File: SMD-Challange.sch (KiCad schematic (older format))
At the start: 19 parts, among them SW1 SW_DPDT_x2, U1 NE555, U2 4017

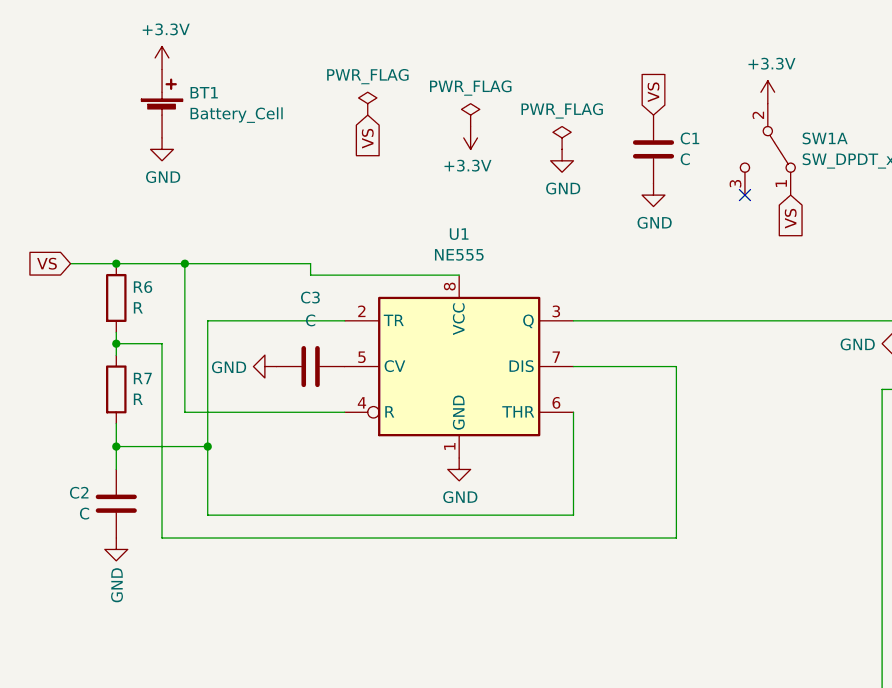
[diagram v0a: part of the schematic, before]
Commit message: update component values for ne555 oscillator
Frequency is now 4.8 Hz

Signed-off-by: Thomas Schmid <tom@binary-kitchen.de>
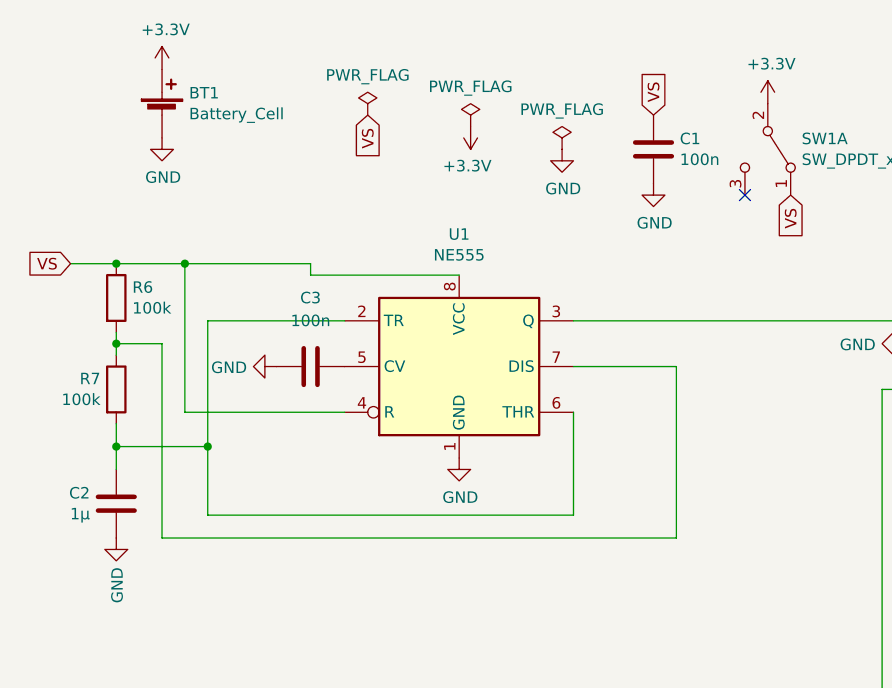
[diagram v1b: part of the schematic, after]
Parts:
- C1, C3: value C -> 100n
- C2: value C -> 1µ
- R6, R7: value R -> 100k
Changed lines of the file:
@@
 P 4600 1500
 F 0 "C1" H 4485 1454 50  0000 R CNN
-F 1 "C" H 4485 1545 50  0000 R CNN
+F 1 "100n" H 4485 1545 50  0000 R CNN
 F 2 "Capacitor_SMD:C_0805_2012Metric_Pad1.15x1.40mm_HandSolder" H 4638 1350 50  0001 C CNN
 F 3 "~" H 4600 1500 50  0001 C CNN
@@
 P 3100 2450
 F 0 "C3" V 2800 2450 50  0000 C CNN
-F 1 "C" V 2900 2450 50  0000 C CNN
+F 1 "100n" V 2900 2450 50  0000 C CNN
 F 2 "Capacitor_SMD:C_0805_2012Metric_Pad1.15x1.40mm_HandSolder" H 3138 2300 50  0001 C CNN
 F 3 "~" H 3100 2450 50  0001 C CNN
@@
 P 2250 2150
 F 0 "R6" H 2320 2196 50  0000 L CNN
-F 1 "R" H 2320 2105 50  0000 L CNN
+F 1 "100k" H 2320 2105 50  0000 L CNN
 F 2 "Resistor_SMD:R_0805_2012Metric_Pad1.15x1.40mm_HandSolder" V 2180 2150 50  0001 C CNN
 F 3 "~" H 2250 2150 50  0001 C CNN
@@
 U 1 1 5BE5B5C6
 P 2250 2550
-F 0 "R7" H 2320 2596 50  0000 L CNN
-F 1 "R" H 2320 2505 50  0000 L CNN
+F 0 "R7" H 2181 2596 50  0000 R CNN
+F 1 "100k" H 2181 2505 50  0000 R CNN
 F 2 "Resistor_SMD:R_0805_2012Metric_Pad1.15x1.40mm_HandSolder" V 2180 2550 50  0001 C CNN
 F 3 "~" H 2250 2550 50  0001 C CNN
@@
 P 2250 3050
 F 0 "C2" H 2365 3004 50  0000 L CNN
-F 1 "C" H 2365 3095 50  0000 L CNN
+F 1 "1µ" H 2365 3095 50  0000 L CNN
 F 2 "Capacitor_SMD:C_0805_2012Metric_Pad1.15x1.40mm_HandSolder" H 2288 2900 50  0001 C CNN
 F 3 "~" H 2250 3050 50  0001 C CNN

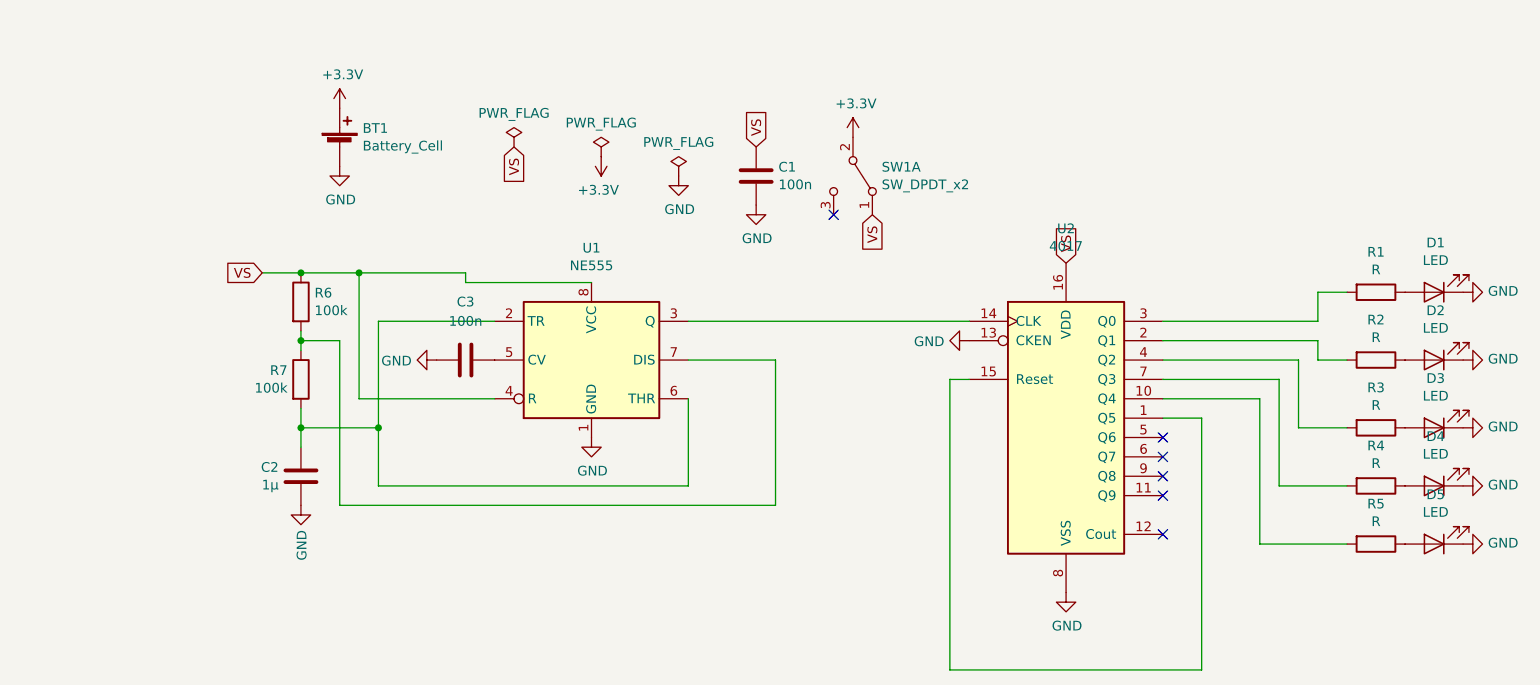
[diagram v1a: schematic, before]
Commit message: cleanup schematic and add title
Signed-off-by: Thomas Schmid <tom@binary-kitchen.de>
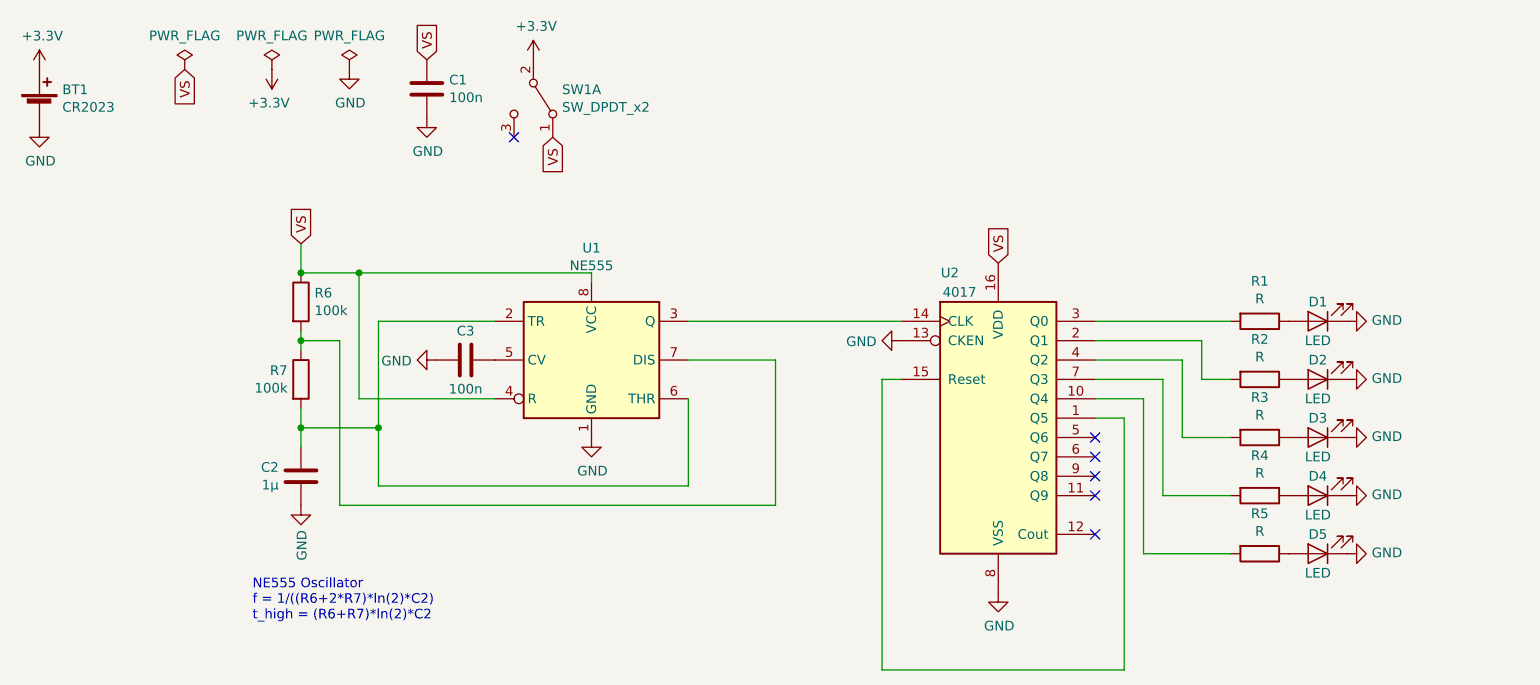
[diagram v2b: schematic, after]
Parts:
- BT1: value Battery_Cell -> CR2023
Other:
- note added: "NE555 Oscillator\nf = 1/((R6+2*R7)*ln(2)*C2)\nt_high = (R6+R7)*ln(2)*C2"
- moved on the sheet: BT1, C1, D1, D2, D3, D4, D5, R1, R2, R3, R4, R5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

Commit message: added custom footprints for smd 0201 and 01005 for hand-soldering
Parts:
- D4, D5: footprint LED_SMD:LED_0201_0603Metric -> SMD-Challange:LED_0201_0603Metric_hand_soldering
- R4: footprint LED_SMD:LED_0201_0603Metric -> SMD-Challange:R_0201_0603Metric_hand_soldering
- R5: footprint LED_SMD:LED_01005_0402Metric -> SMD-Challange:R_01005_0402Metric_hand_soldering
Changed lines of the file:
@@
 F 0 "D4" H 7500 3050 50  0000 C CNN
 F 1 "LED" H 7500 3250 50  0000 C CNN
-F 2 "LED_SMD:LED_0201_0603Metric" H 7500 3150 50  0001 C CNN
+F 2 "SMD-Challange:LED_0201_0603Metric_hand_soldering" H 7500 3150 50  0001 C CNN
 F 3 "~" H 7500 3150 50  0001 C CNN
 	1    7500 3150
@@
 F 0 "D5" H 7500 3350 50  0000 C CNN
 F 1 "LED" H 7500 3550 50  0000 C CNN
-F 2 "LED_SMD:LED_0201_0603Metric" H 7500 3450 50  0001 C CNN
+F 2 "SMD-Challange:LED_0201_0603Metric_hand_soldering" H 7500 3450 50  0001 C CNN
 F 3 "~" H 7500 3450 50  0001 C CNN
 	1    7500 3450
@@
 F 0 "R4" V 6993 3150 50  0000 C CNN
 F 1 "R" V 7084 3150 50  0000 C CNN
-F 2 "LED_SMD:LED_0201_0603Metric" V 7130 3150 50  0001 C CNN
+F 2 "SMD-Challange:R_0201_0603Metric_hand_soldering" V 7130 3150 50  0001 C CNN
 F 3 "~" H 7200 3150 50  0001 C CNN
 	1    7200 3150
@@
 F 0 "R5" V 6993 3450 50  0000 C CNN
 F 1 "R" V 7084 3450 50  0000 C CNN
-F 2 "LED_SMD:LED_01005_0402Metric" V 7130 3450 50  0001 C CNN
+F 2 "SMD-Challange:R_01005_0402Metric_hand_soldering" V 7130 3450 50  0001 C CNN
 F 3 "~" H 7200 3450 50  0001 C CNN
 	1    7200 3450

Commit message: changed some footprints and made the surface printing nicer
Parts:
- D1: footprint LED_SMD:LED_0805_2012Metric_Pad1.15x1.40mm_HandSolder -> SMD-Challange:LED_0805_2012Metric_Pad1.15x1.40mm_HandSolder_simple_drawing
- D2: footprint LED_SMD:LED_0603_1608Metric_Pad1.05x0.95mm_HandSolder -> SMD-Challange:LED_0603_1608Metric_Pad1.05x0.95mm_HandSolder_simple_drawing
- R1: footprint LED_SMD:LED_0805_2012Metric_Pad1.15x1.40mm_HandSolder -> Resistor_SMD:R_0805_2012Metric_Pad1.15x1.40mm_HandSolder
- R2: footprint LED_SMD:LED_0603_1608Metric_Pad1.05x0.95mm_HandSolder -> Resistor_SMD:R_0603_1608Metric_Pad1.05x0.95mm_HandSolder
- R3: footprint LED_SMD:LED_0402_1005Metric -> Resistor_SMD:R_0402_1005Metric
- U2: footprint Package_SO:SOP-16_4.4x10.4mm_P1.27mm -> SMD-Challange:SOP-16_4.4x10.4mm_P1.27mm_simple_drawing
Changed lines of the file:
@@
 F 0 "D1" H 7500 2150 50  0000 C CNN
 F 1 "LED" H 7500 2350 50  0000 C CNN
-F 2 "LED_SMD:LED_0805_2012Metric_Pad1.15x1.40mm_HandSolder" H 7500 2250 50  0001 C CNN
+F 2 "SMD-Challange:LED_0805_2012Metric_Pad1.15x1.40mm_HandSolder_simple_drawing" H 7500 2250 50  0001 C CNN
 F 3 "~" H 7500 2250 50  0001 C CNN
 	1    7500 2250
@@
 F 0 "D2" H 7500 2450 50  0000 C CNN
 F 1 "LED" H 7500 2650 50  0000 C CNN
-F 2 "LED_SMD:LED_0603_1608Metric_Pad1.05x0.95mm_HandSolder" H 7500 2550 50  0001 C CNN
+F 2 "SMD-Challange:LED_0603_1608Metric_Pad1.05x0.95mm_HandSolder_simple_drawing" H 7500 2550 50  0001 C CNN
 F 3 "~" H 7500 2550 50  0001 C CNN
 	1    7500 2550
@@
 F 0 "R1" V 6993 2250 50  0000 C CNN
 F 1 "R" V 7084 2250 50  0000 C CNN
-F 2 "LED_SMD:LED_0805_2012Metric_Pad1.15x1.40mm_HandSolder" V 7130 2250 50  0001 C CNN
+F 2 "Resistor_SMD:R_0805_2012Metric_Pad1.15x1.40mm_HandSolder" V 7130 2250 50  0001 C CNN
 F 3 "~" H 7200 2250 50  0001 C CNN
 	1    7200 2250
@@
 F 0 "R2" V 6993 2550 50  0000 C CNN
 F 1 "R" V 7084 2550 50  0000 C CNN
-F 2 "LED_SMD:LED_0603_1608Metric_Pad1.05x0.95mm_HandSolder" V 7130 2550 50  0001 C CNN
+F 2 "Resistor_SMD:R_0603_1608Metric_Pad1.05x0.95mm_HandSolder" V 7130 2550 50  0001 C CNN
 F 3 "~" H 7200 2550 50  0001 C CNN
 	1    7200 2550
@@
 F 0 "R3" V 6993 2850 50  0000 C CNN
 F 1 "R" V 7084 2850 50  0000 C CNN
-F 2 "LED_SMD:LED_0402_1005Metric" V 7130 2850 50  0001 C CNN
+F 2 "Resistor_SMD:R_0402_1005Metric" V 7130 2850 50  0001 C CNN
 F 3 "~" H 7200 2850 50  0001 C CNN
 	1    7200 2850
@@
 F 0 "U2" H 5600 3500 50  0000 C CNN
 F 1 "4017" H 5650 3400 50  0000 C CNN
-F 2 "Package_SO:SOP-16_4.4x10.4mm_P1.27mm" H 5850 2750 50  0001 C CNN
+F 2 "SMD-Challange:SOP-16_4.4x10.4mm_P1.27mm_simple_drawing" H 5850 2750 50  0001 C CNN
 F 3 "http://www.intersil.com/content/dam/Intersil/documents/cd40/cd4017bms-22bms.pdf" H 5850 2750 50  0001 C CNN
 	1    5850 2750

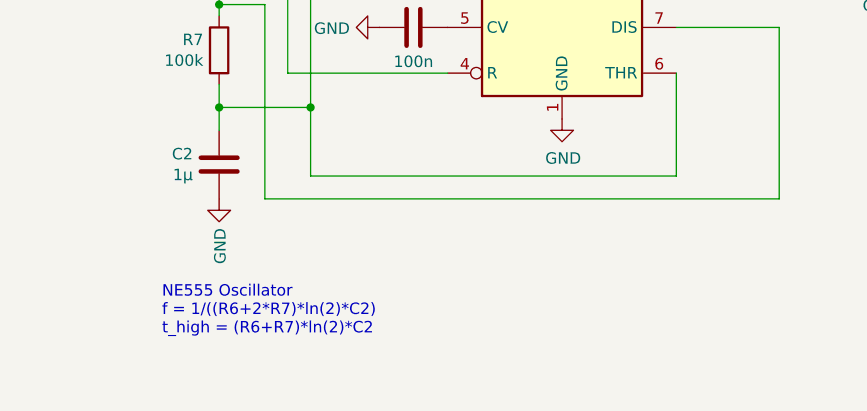
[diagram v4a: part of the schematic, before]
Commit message: add logo to site layout and update description
Signed-off-by: Thomas Schmid <tom@binary-kitchen.de>
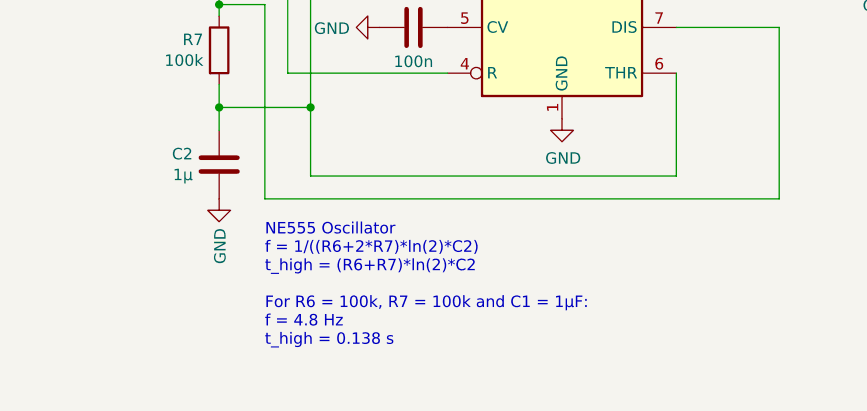
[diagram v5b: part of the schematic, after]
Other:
- note added: "NE555 Oscillator\nf = 1/((R6+2*R7)*ln(2)*C2)\nt_high = (R6+R7)*ln(2)*C2\n\nFor R6 = 100k, R7 = 100k and C1 = 1µF:\nf = 4.8 Hz\nt_high = 0.138 s\n"
- note removed: "NE555 Oscillator\nf = 1/((R6+2*R7)*ln(2)*C2)\nt_high = (R6+R7)*ln(2)*C2"
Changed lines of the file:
@@
 encoding utf-8
 Sheet 1 1
-Title "Binary Kitchen SMD Soldering Challenge"
+Title "Nibble++"
 Date "2018-11-11"
-Rev "A"
+Rev "V1.0"
 Comp "Binary Kitchen e.V."
 Comment1 ""
@@
 	1    0    0    -1
 $EndComp
-Text Notes 2000 3800 0    50   ~ 0
-NE555 Oscillator\nf = 1/((R6+2*R7)*ln(2)*C2)\nt_high = (R6+R7)*ln(2)*C2
+Text Notes 2450 3850 0    50   ~ 0
+NE555 Oscillator\nf = 1/((R6+2*R7)*ln(2)*C2)\nt_high = (R6+R7)*ln(2)*C2\n\nFor R6 = 100k, R7 = 100k and C1 = 1µF:\nf = 4.8 Hz\nt_high = 0.138 s\n
 Wire Wire Line
 	6350 2250 7050 2250

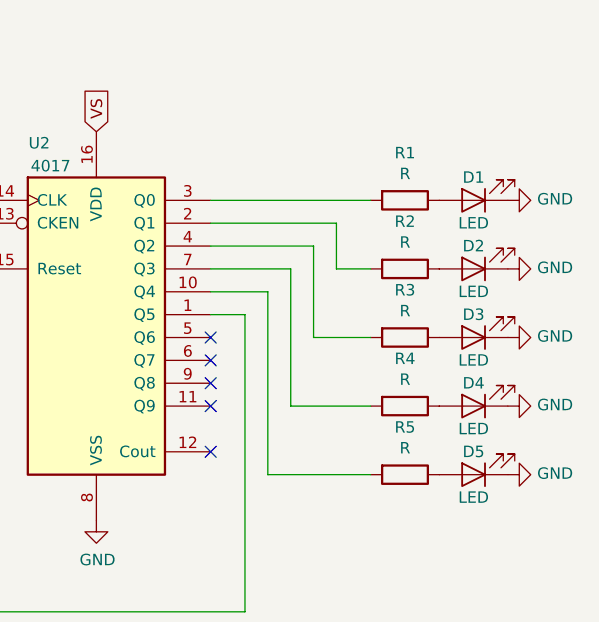
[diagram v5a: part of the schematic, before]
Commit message: remove some silkscreen features and cleanup layout
Signed-off-by: Thomas Schmid <tom@binary-kitchen.de>
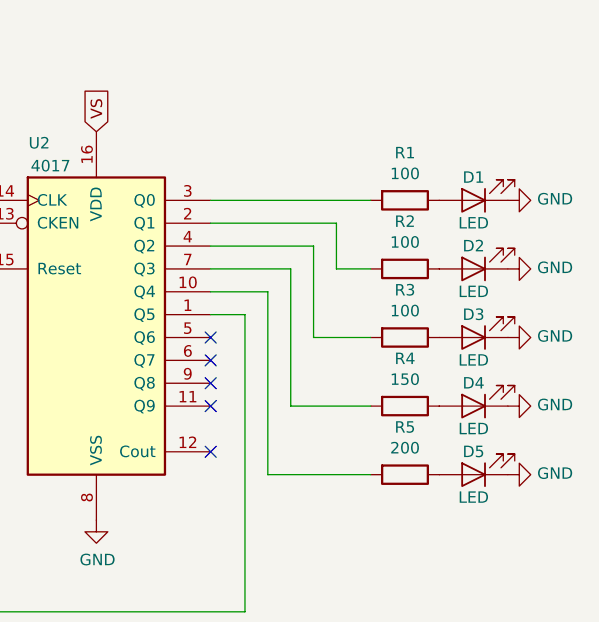
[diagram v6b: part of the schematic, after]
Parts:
- R1, R2, R3: value R -> 100
- R4: value R -> 150
- R5: value R -> 200
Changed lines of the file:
@@
 P 7200 2250
 F 0 "R1" V 6993 2250 50  0000 C CNN
-F 1 "R" V 7084 2250 50  0000 C CNN
+F 1 "100" V 7084 2250 50  0000 C CNN
 F 2 "Resistor_SMD:R_0805_2012Metric_Pad1.15x1.40mm_HandSolder" V 7130 2250 50  0001 C CNN
 F 3 "~" H 7200 2250 50  0001 C CNN
@@
 P 7200 2550
 F 0 "R2" V 6993 2550 50  0000 C CNN
-F 1 "R" V 7084 2550 50  0000 C CNN
+F 1 "100" V 7084 2550 50  0000 C CNN
 F 2 "Resistor_SMD:R_0603_1608Metric_Pad1.05x0.95mm_HandSolder" V 7130 2550 50  0001 C CNN
 F 3 "~" H 7200 2550 50  0001 C CNN
@@
 P 7200 2850
 F 0 "R3" V 6993 2850 50  0000 C CNN
-F 1 "R" V 7084 2850 50  0000 C CNN
+F 1 "100" V 7084 2850 50  0000 C CNN
 F 2 "Resistor_SMD:R_0402_1005Metric" V 7130 2850 50  0001 C CNN
 F 3 "~" H 7200 2850 50  0001 C CNN
@@
 P 7200 3150
 F 0 "R4" V 6993 3150 50  0000 C CNN
-F 1 "R" V 7084 3150 50  0000 C CNN
+F 1 "150" V 7084 3150 50  0000 C CNN
 F 2 "SMD-Challange:R_0201_0603Metric_hand_soldering" V 7130 3150 50  0001 C CNN
 F 3 "~" H 7200 3150 50  0001 C CNN
@@
 P 7200 3450
 F 0 "R5" V 6993 3450 50  0000 C CNN
-F 1 "R" V 7084 3450 50  0000 C CNN
+F 1 "200" V 7084 3450 50  0000 C CNN
 F 2 "SMD-Challange:R_01005_0402Metric_hand_soldering" V 7130 3450 50  0001 C CNN
 F 3 "~" H 7200 3450 50  0001 C CNN
